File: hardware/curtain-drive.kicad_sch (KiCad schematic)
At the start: 46 parts, among them J1 DC IN 12V, J2 USB-C, J3 MOTOR, J4 ENCODER I2C, SW1 USER, SW2 BOOT, SW3 RESET, U1 ESP32-C3-WROOM-02, U2 DRV8876PWP, U3 AP63203WU, U4 USBLC6-2SC6

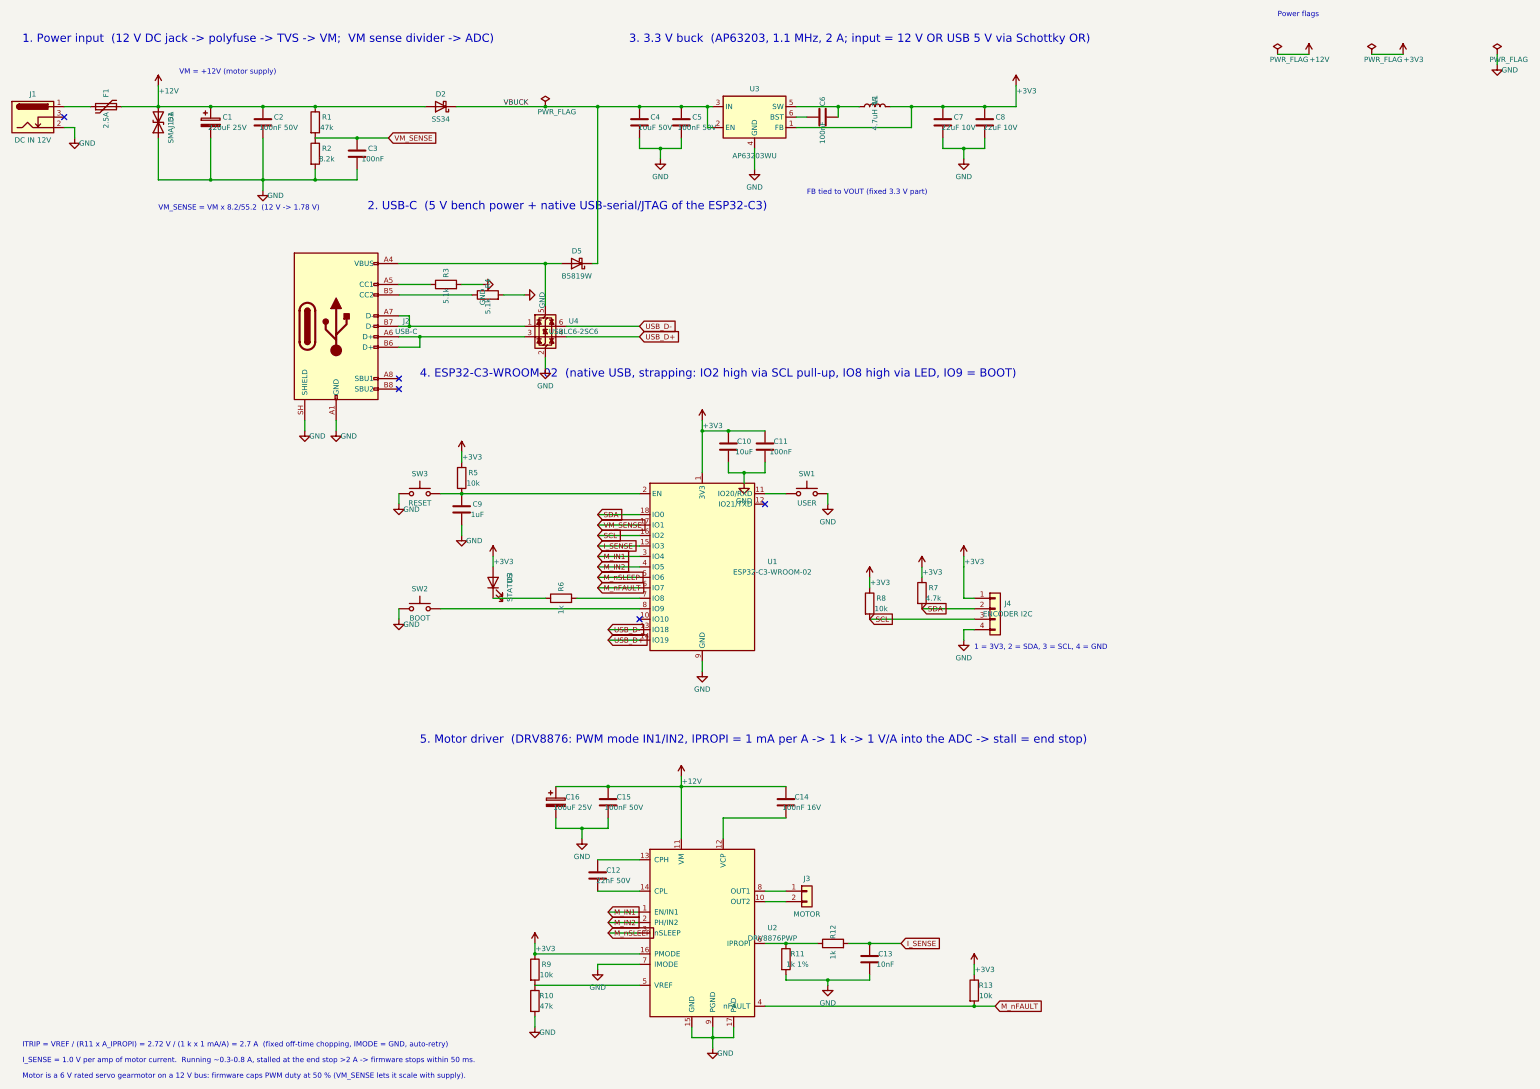
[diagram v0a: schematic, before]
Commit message: Rev B through-hole board, rev A fixes, enclosure and renders
Rev B (hardware-revB/): same circuit and ESP32-C3 as rev A, but every
passive, diode, LED, switch and header is a through-hole part stocked by
the DTU component shop. Still single-sided with no vias: SMD parts on
F.Cu, THT bodies on the back. 90x72 mm, DRC clean. BOM mapped to shop
rows in docs/revB-bom.md.

Rev A: single-sided, via-free layout for the xTool fiber laser; D1 TVS
turned the right way round (cathode on +12V); R8 SCL pull-up 4.7k to
match SDA; production DXFs and drill.

Enclosure: Blender model, 3D board exports, showcase renders and GIFs.
Firmware: pin map for the new layout, vm_divider substitution.
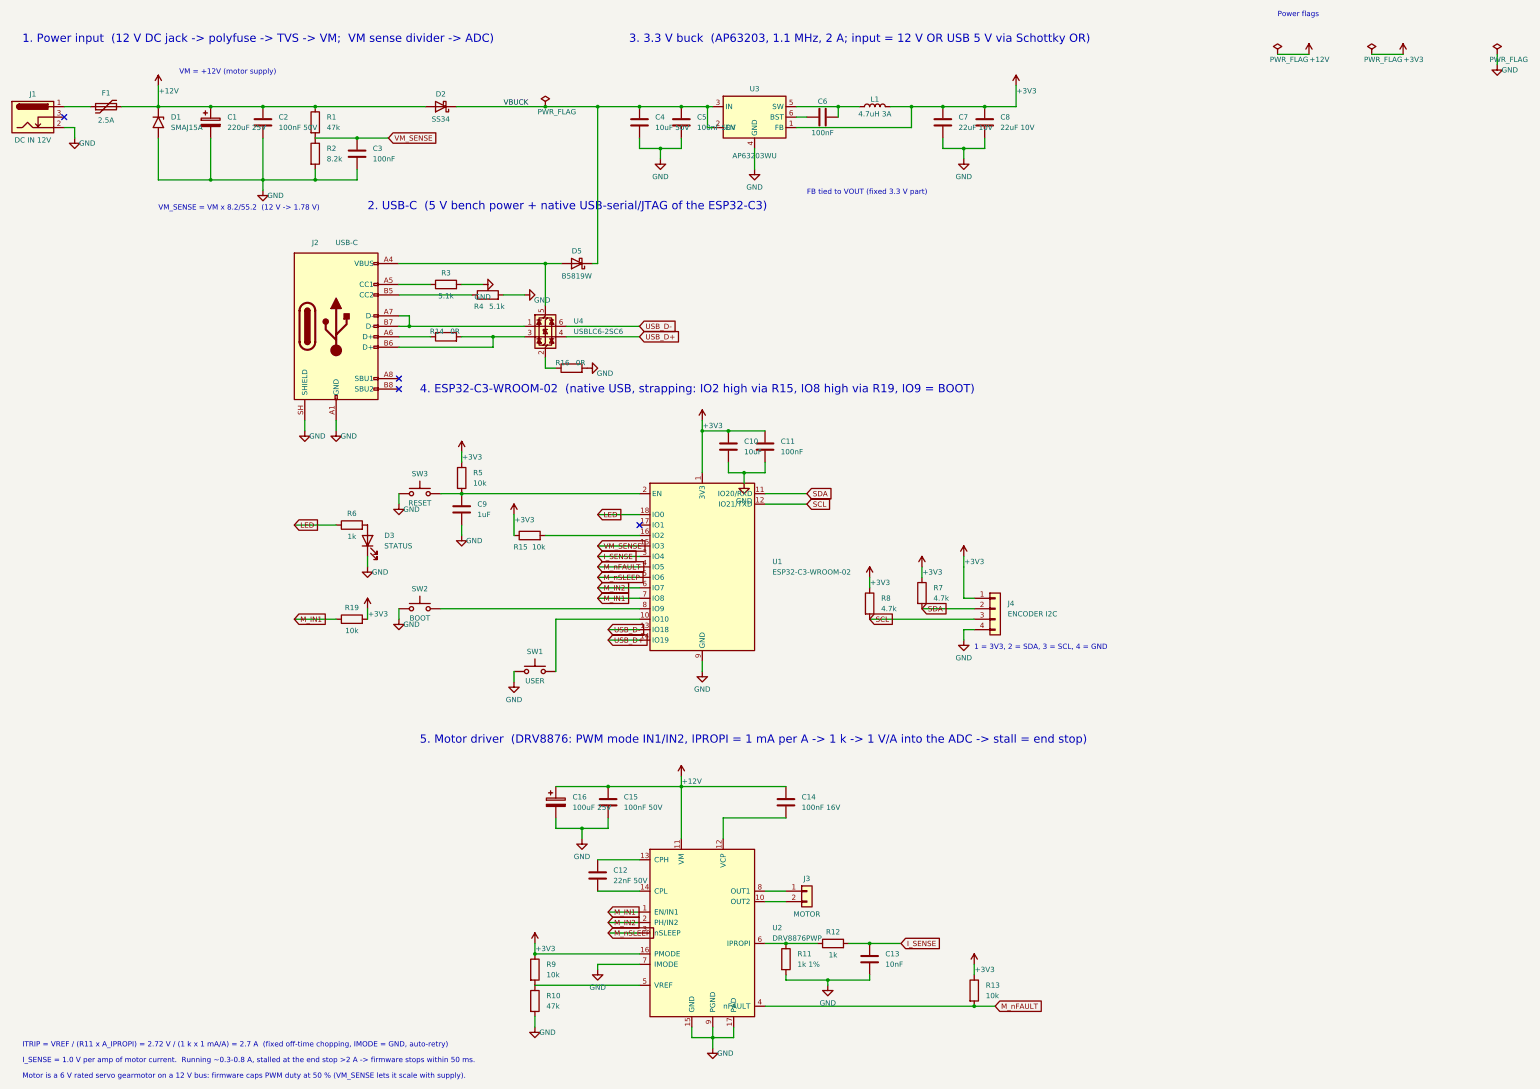
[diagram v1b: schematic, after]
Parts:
- removed D1: SMAJ15A, Diode_SMD:D_SMA, symbol Device:D_TVS
- added D1: SMAJ15A, Diode_SMD:D_SMA, symbol Diode:SMAJ15A
- added R14: 0R, Resistor_SMD:R_0603_1608Metric, symbol Device:R
- added R15, R19: 10k, Resistor_SMD:R_0603_1608Metric, symbol Device:R
- added R16: 0R, Resistor_SMD:R_0805_2012Metric, symbol Device:R
- J1: footprint Connector_BarrelJack:BarrelJack_Horizontal -> Connector_BarrelJack:BarrelJack_CUI_PJ-036AH-SMT_Horizontal
- J2: footprint Connector_USB:USB_C_Receptacle_HRO_TYPE-C-31-M-12 -> CurtainDrive:USB_C_Receptacle_HRO_TYPE-C-31-M-12_1L
- J3: footprint Connector_JST:JST_XH_B2B-XH-A_1x02_P2.50mm_Vertical -> Connector_JST:JST_PH_B2B-PH-SM4-TB_1x02-1MP_P2.00mm_Vertical
- J4: footprint Connector_JST:JST_XH_B4B-XH-A_1x04_P2.50mm_Vertical -> Connector_JST:JST_PH_B4B-PH-SM4-TB_1x04-1MP_P2.00mm_Vertical
- R1: footprint Resistor_SMD:R_0603_1608Metric -> Resistor_SMD:R_1206_3216Metric
- R10, R13, R3, R9: footprint Resistor_SMD:R_0603_1608Metric -> Resistor_SMD:R_0805_2012Metric
- R8: value 10k -> 4.7k
- SW1, SW2, SW3: footprint Button_Switch_SMD:SW_SPST_PTS645Sx43SMTR92 -> CurtainDrive:SW_SPST_PTS645Sx43SMTR92_Jumpers
- U1: footprint RF_Module:ESP32-C3-WROOM-02 -> CurtainDrive:ESP32-C3-WROOM-02_NoVias
- U2: footprint Package_SO:HTSSOP-16-1EP_4.4x5mm_P0.65mm_EP3.4x5mm_Mask2.46x2.31mm_ThermalVias -> Package_SO:HTSSOP-16-1EP_4.4x5mm_P0.65mm_EP3.4x5mm_Mask2.46x2.31mm
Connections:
- net +12V: now also D1.1 (A1)
- net +3V3: now also R15.1, R19.2; no longer D3.2 (A)
- net GND: now also D3.1 (K), SW1.1, D1.2 (A2), R16.2; no longer SW1.2, U4.2 (GND)
- net I_SENSE: now also U1.3 (IO4); no longer U1.15 (IO3)
- net M_IN1: now also U1.7 (IO8), R19.1; no longer U1.3 (IO4)
- net M_IN2: now also U1.6 (IO7); no longer U1.4 (IO5)
- net M_nFAULT: now also U1.4 (IO5); no longer U1.6 (IO7)
- net SCL: now also U1.12 (IO21/TXD); no longer U1.16 (IO2)
- net SDA: now also U1.11 (IO20/RXD); no longer U1.18 (IO0)
- net VM_SENSE: now also U1.15 (IO3); no longer U1.17 (IO1)
- net at J2.B6 (D+), U4.3 (I/O2): now also R14.2; no longer J2.A6 (D+)
- net LED: now reaches R6.1
- net LED: now also U1.18 (IO0); no longer D3.1 (K)
- net at R6.2: now also D3.2 (A); no longer U1.7 (IO8)
- net at U1.10 (IO10): now also SW1.2
- new net: R16.1, U4.2 (GND)
- new net: J2.A6 (D+), R14.1
- new net: R15.2, U1.16 (IO2)
- no-connect marks 5 -> 4
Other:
- note added: "4. ESP32-C3-WROOM-02 (native USB, strapping: IO2 high via R15, IO8 high via R19, IO9 = BOOT)"
- note removed: "4. ESP32-C3-WROOM-02 (native USB, strapping: IO2 high via SCL pull-up, IO8 high via LED, IO9 = BOOT)"
